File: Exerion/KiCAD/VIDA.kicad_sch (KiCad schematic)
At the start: 45 parts, among them U11T_1 74LS32, U2 74LS04, U2N1 74LS245, U2R1 74LS374, U3 74LS245, U3M1 74LS138, U3P1 74LS138, U3R_1 74LS139, U3S1 74LS02, U3S_1 74LS02, U4 74LS14, U4N_1 HM6116P-3, U4P1 27128, U4S1 2764, U56R1 Z80CPUA, U5P1 74LS245, U6K1 2764, U6LM1 74LS374, U6N1 HM6116P-3, U6P1 74LS367, U7K1 74LS374, U7L1 74LS175, U7M1 74LS157, U7N_1 74LS86, U7R1 74LS157, U7S_1 74LS86, U7T_1 74LS08, U7U_1 74LS32, U8H3 74LS161, U8J_1 74LS86, U8K1 74LS253, U8L1 82S126-9 / 6301, U8M1 74LS157, U8N_1 74LS86, U8R1 74LS161, U8S1 74LS161, U8T_1 74LS74, U8V_1 74LS00, U9M_1 74LS74, U9N1 74LS161, U9P_1 74LS04, U9R 74LS138, U9S 74LS138, U9T_1 74LS32, U9U_2 74LS86

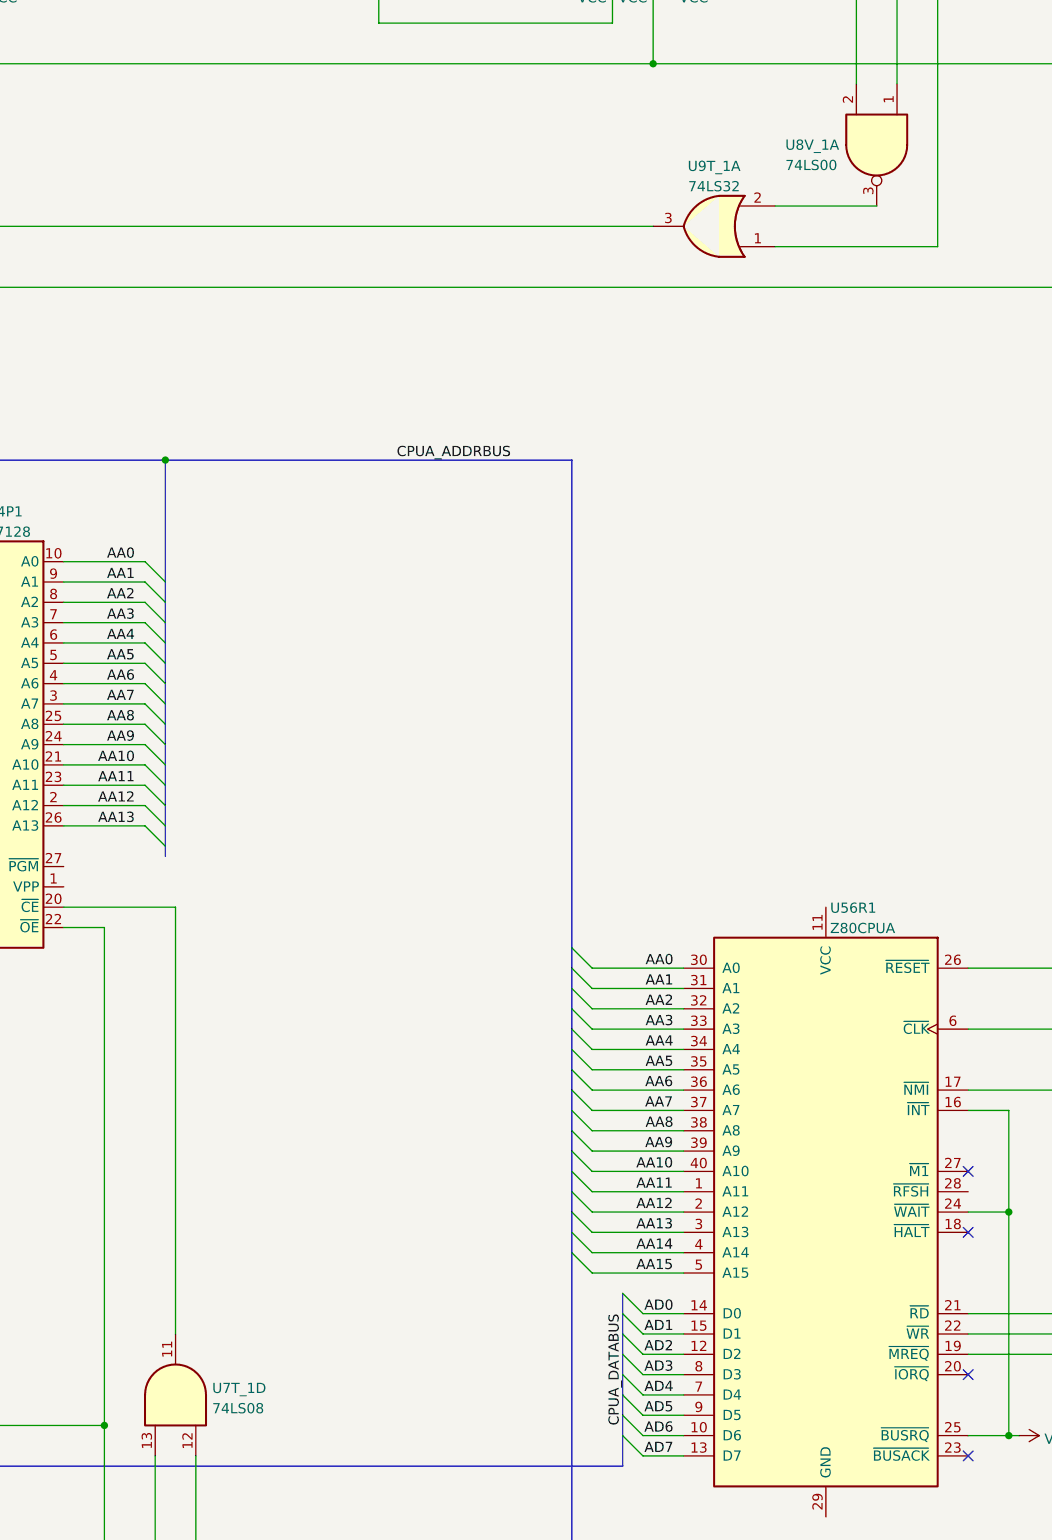
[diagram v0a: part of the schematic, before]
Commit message: Component naming updates
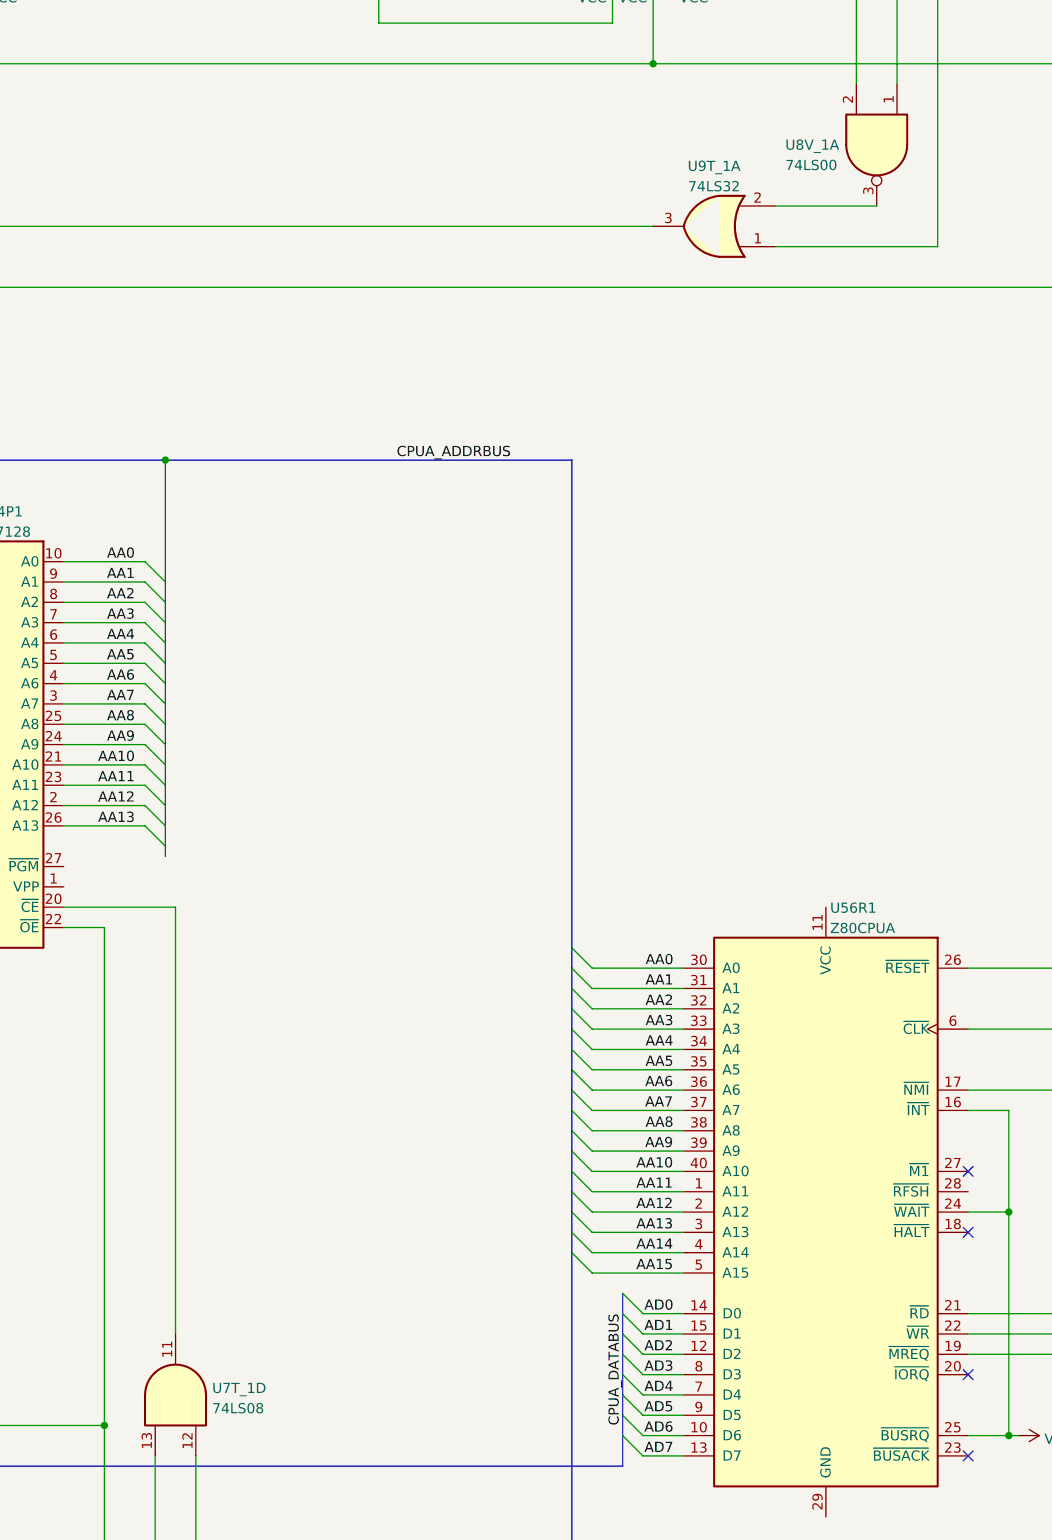
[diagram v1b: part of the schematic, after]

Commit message: Exerion Updates to KiCAD 8
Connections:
- net D0: now also U2R1.18 (D7); no longer U2R1.3 (D0)
- net D1: now also U2R1.3 (D0); no longer U2R1.4 (D1)
- net D2: now also U2R1.4 (D1); no longer U2R1.7 (D2)
- net D3: now also U2R1.17 (D6); no longer U2R1.8 (D3)
- net D4: now also U2R1.14 (D5); no longer U2R1.13 (D4)
- net D5: now also U2R1.7 (D2); no longer U2R1.14 (D5)
- net D6: now also U2R1.8 (D3); no longer U2R1.17 (D6)
- net D7: now also U2R1.13 (D4); no longer U2R1.18 (D7)
